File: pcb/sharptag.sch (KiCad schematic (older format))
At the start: 10 parts

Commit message: Layout almost complete. Needs tooling holes.
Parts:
- removed U?: ESP-PSRAM32, Package_SO:SOIC-8_3.9x4.9mm_P1.27mm, symbol Memory_RAM:ESP-PSRAM32
- removed U?: W25Q128JVS, Package_SO:SOIC-8_5.23x5.23mm_P1.27mm, symbol Memory_Flash:W25Q128JVS
- added C1, C14, C15, C18, C20, C3, C6, C7: 100n, Capacitor_SMD:C_0603_1608Metric, symbol Device:C
- added C10, C12, C23, C4: 1u, Capacitor_SMD:C_0603_1608Metric, symbol Device:C
- added C11, C2, C22, C5, C8: 10u, Capacitor_SMD:C_0805_2012Metric, symbol Device:C
- added C13, C19: 2.2u, Capacitor_SMD:C_1206_3216Metric, symbol Device:C
- added C16: 2.2n, Capacitor_SMD:C_0603_1608Metric, symbol Device:C
- added C17: 2.2u, Capacitor_SMD:C_0805_2012Metric, symbol Device:C
- added C21, C9: 22u, Capacitor_SMD:C_0805_2012Metric, symbol Device:C
- added D10, D7, D8, D9: WS2812B, LED_SMD:LED_WS2812B_PLCC4_5.0x5.0mm_P3.2mm, symbol LED:WS2812B
- added D11, D12: ZMM3V3, Diode_SMD:D_MiniMELF, symbol Device:D_Zener
- added D3: B5819W, Diode_SMD:D_SOD-123, symbol Diode:1N5819
- added D4, D5, D6: LED, LED_SMD:LED_0603_1608Metric, symbol Device:LED
- added H1, H2, H3, H4: MountingHole, MountingHole:MountingHole_3.2mm_M3_DIN965, symbol Mechanical:MountingHole
- added J2: Conn_01x10, Connector_FFC-FPC:TE_1-1734839-0_1x10-1MP_P0.5mm_Horizontal, symbol Connector_Generic:Conn_01x10
- added J3: Conn_01x02, Connector_JST:JST_PH_S2B-PH-SM4-TB_1x02-1MP_P2.00mm_Horizontal, symbol Connector_Generic:Conn_01x02
- added J4: Conn_01x04, Connector_JST:JST_SH_SM04B-SRSS-TB_1x04-1MP_P1.00mm_Horizontal, symbol Connector_Generic:Conn_01x04
- added J5, J6: Conn_01x03, Connector_JST:JST_PH_S3B-PH-SM4-TB_1x03-1MP_P2.00mm_Horizontal, symbol Connector_Generic:Conn_01x03
- added JP1: SolderJumper_2_Bridged, Jumper:SolderJumper-2_P1.3mm_Bridged2Bar_RoundedPad1.0x1.5mm, symbol Jumper:SolderJumper_2_Bridged
- added LS1: Speaker, Buzzer_Beeper:MagneticBuzzer_Kobitone_254-EMB84Q-RO, symbol Device:Speaker
- added Q1, Q2, Q3: DMG3415U-7, Package_TO_SOT_SMD:SOT-23, symbol Transistor_FET:DMG2301L
- added Q4: Q_Photo_NPN, Diode_SMD:D_0603_1608Metric, symbol Device:Q_Photo_NPN
- added R1, R10, R16, R22, R23, R26, R3, R5, R8: 10k, Resistor_SMD:R_0603_1608Metric, symbol Device:R
- added R11, R12, R15, R25: 100K, Resistor_SMD:R_0603_1608Metric, symbol Device:R
- added R13, R14, R18: 47k, Resistor_SMD:R_0603_1608Metric, symbol Device:R
- added R17, R20, R21: 1M, Resistor_SMD:R_0603_1608Metric, symbol Device:R
- added R19, R2, R27, R28, R6: 1K, Resistor_SMD:R_0603_1608Metric, symbol Device:R
- added R24: 2.4k, Resistor_SMD:R_0603_1608Metric, symbol Device:R
- added SW1, SW2, SW3, SW4, SW5, SW6: SW_Push, Button_Switch_SMD:SW_SPST_CK_RS282G05A3, symbol Switch:SW_Push
- added SW7: SW_SPDT, Button_Switch_SMD:SW_SPDT_PCM12, symbol Switch:SW_SPDT
- added U2: PAM8302AAS, Package_SO:MSOP-8_3x3mm_P0.65mm, symbol Amplifier_Audio:PAM8302AAS
- added U3: AP2112K-3.3, Package_TO_SOT_SMD:SOT-23-5, symbol Regulator_Linear:AP2112K-3.3
- added U5: MPU-6050, Sensor_Motion:InvenSense_QFN-24_4x4mm_P0.5mm, symbol Sensor_Motion:MPU-6050
- added U6: REG710NA-5, Package_TO_SOT_SMD:SOT-23-6, symbol reg710na:REG710NA-5
- added U7: TPL5110, Package_TO_SOT_SMD:SOT-23-6, symbol Timer:TPL5110
- D1: renamed from D?; LCSC (none) -> C72038
- D2: renamed from D?; LCSC (none) -> C72041
- J1: renamed from J?; footprint (none) -> Connector_USB:USB_C_Receptacle_HRO_TYPE-C-31-M-12; symbol Connector:USB_C_Receptacle_USB2.0 -> sharptag-rescue:USB_C_Receptacle_USB2.0-Connector; LCSC (none) -> C165948
- gave numbers to parts that had none: 5
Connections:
- net BATT_MON: now also U4.18 (IO15), C14.1, R20.1, R21.2; no longer U4.7 (IO04)
- net BOOT0: now also SW2.2
- net D13: now also R16.1
- net GND: now also J1.S1 (SHIELD), C1.2, C10.2, C11.2, C12.2, C13.2, C14.2, C15.2, C16.2, C18.2, C19.2, C2.2, C20.2, C21.2, C22.2, C23.2, C3.2, C4.2, C5.2, C7.2, C8.2, C9.2, D10.3 (VSS), D11.2 (A), D12.2 (A), D4.1 (K), D5.1 (K), D6.1 (K), D7.3 (VSS), D8.3 (VSS), D9.3 (VSS), J2.10 (Pin_10), J2.9 (Pin_9), J3.2 (Pin_2), J4.1 (Pin_1), J5.1 (Pin_1), J6.1 (Pin_1), R11.1, R15.2, R17.1, R21.1, R24.2, R26.2, SW1.1, SW2.1, SW3.1, SW4.1, SW5.1, SW6.1, SW7.2 (B), U2.7 (GND), U3.2 (GND), U5.18 (GND), U6.2 (GND), U7.2 (GND), U7.4 (DONE)
- net IO38_DBLTAP: now also C12.1, R17.2
- net RESET: now also R1.2, SW1.2
- net SCL: now also U4.36 (IO42), J4.4 (Pin_4), R22.2, U5.23 (SCL); no longer U4.28 (IO34)
- net SDA: now also U4.35 (IO41), J4.3 (Pin_3), R23.2, U5.24 (SDA); no longer U4.27 (IO33)
- net SPKR_SD: now reaches U4.19 (IO16)
- net SPKR_SD: now also R15.1, U2.1 (~SD)
- net +3V3: now reaches U4.2 (3V3)
- net +3V3: now also C13.1, C18.1, C20.1, C9.1, J4.2 (Pin_2), J5.2 (Pin_2), J6.2 (Pin_2), JP1.1 (A), Q3.2 (S), R1.1, R10.1, R22.1, R23.1, R25.2, R3.1, R5.1, R8.1, U3.5 (VOUT), U5.13 (VDD), U5.8 (VDDIO), U6.3 (EN), U6.5 (VIN), U7.1 (VDD), U7.6 (EN/ONE_SHOT)
- net AUDIO: now reaches U4.20 (IO17)
- net AUDIO: now also C6.1
- net AD1: now reaches U4.21 (IO18)
- net AD1: now also D12.1 (K), R28.2
- net BUTTON1: now reaches U4.24 (IO21)
- net BUTTON1: now also R5.2, SW4.2
- net BUTTON0: now reaches U4.25 (IO26)
- net BUTTON0: now also R3.2, SW3.2
- net NEOPOWER: now reaches U4.33 (IO39)
- net NEOPOWER: now also Q3.1 (G), R25.1
- net NEOPIXEL: now reaches U4.39 (IO45)
- net NEOPIXEL: now also D7.4 (DIN)
- net BUTTON3: now reaches U4.4 (IO01)
- net BUTTON3: now also R10.2, SW6.2
- net BUTTON2: now reaches U4.5 (IO02)
- net BUTTON2: now also R8.2, SW5.2
- net LIGHT: now reaches U4.6 (IO03)
- net LIGHT: now also Q4.2 (E), R26.1
- net VBUS: now reaches J1.A4 (VBUS), J1.A9 (VBUS), J1.B4 (VBUS), J1.B9 (VBUS)
- net VBUS: now also U1.4 (VCC), C21.1, C5.1, D3.2 (A), Q1.1 (G), R11.2, R19.2, R2.1, R6.2
- net VBAT: now reaches U1.3 (BAT)
- net VBAT: now also C2.1, J3.1 (Pin_1), Q1.3 (D), R20.2
- net at D1.2 (A): now also R2.2; no longer D2.2 (A)
- net MISO renamed CIPO
- net MOSI renamed LCD_DAT
- net LCD_DAT: now also J2.2 (Pin_2)
- net SCK renamed LCD_CS
- net LCD_CS: now also J2.3 (Pin_3)
- new net: D2.2 (A), R6.1
- new net: Q2.1 (G), R12.1, SW7.3 (C)
- new net: D3.1 (K), Q1.2 (S), Q2.2 (S), R12.2
- new net: C17.2, U6.4 (CPUMP-)
- new net: C17.1, U6.6 (CPUMP+)
- new net: C15.1, U5.10 (REGOUT)
- new net: C16.1, U5.20 (CPOUT)
- new net: R13.2, U2.3 (IN+)
- new net: R14.2, U2.4 (IN-)
- new net: LS1.1, U2.5 (OUT+)
- new net: LS1.2, U2.8 (OUT-)
- new net: J5.3 (Pin_3), R27.1
- new net: J6.3 (Pin_3), R28.1
- new net: C7.1, R14.1
- new net: C6.2, R13.1
- new net: D4.2 (A), R16.2
- new net: D5.2 (A), R18.2
- new net: JP1.2 (B), R18.1
- new net: D6.2 (A), R19.1
- new net: D7.2 (DOUT), D8.4 (DIN)
- new net: D8.2 (DOUT), D9.4 (DIN)
- new net: D10.4 (DIN), D9.2 (DOUT)
- new net: R24.1, U7.3 (DELAY/M_DRV)
- new net +5V: C1.1, C19.1, C3.1, C4.1, J2.5 (Pin_5), J2.6 (Pin_6), J2.7 (Pin_7), J2.8 (Pin_8), U6.1 (VOUT)
- new net D1: D11.1 (K), R27.2, U4.27 (IO33)
- new net EXTCOMIN: J2.4 (Pin_4), U7.5 (DRV)
- new net LCD_CLK: J2.1 (Pin_1), U4.28 (IO34)
- new net VDD: C10.1, C11.1, C8.1, Q2.3 (D), U2.6 (VDD), U3.1 (VIN), U3.3 (EN)
- new net VNEO: C22.1, C23.1, D10.1 (VDD), D7.1 (VDD), D8.1 (VDD), D9.1 (VDD), Q3.3 (D), Q4.1 (C)
- no-connect marks 1 -> 8
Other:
- moved on the sheet: D1, D2, J1, R4, R7, R9, U1, U4

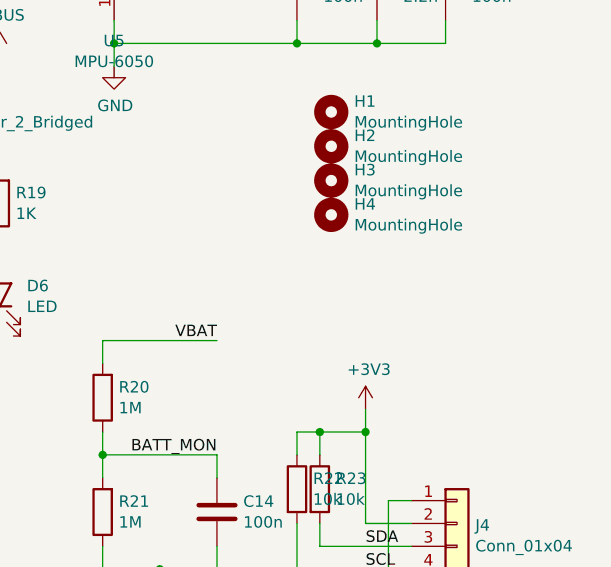
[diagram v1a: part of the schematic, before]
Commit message: Added tooling holes.
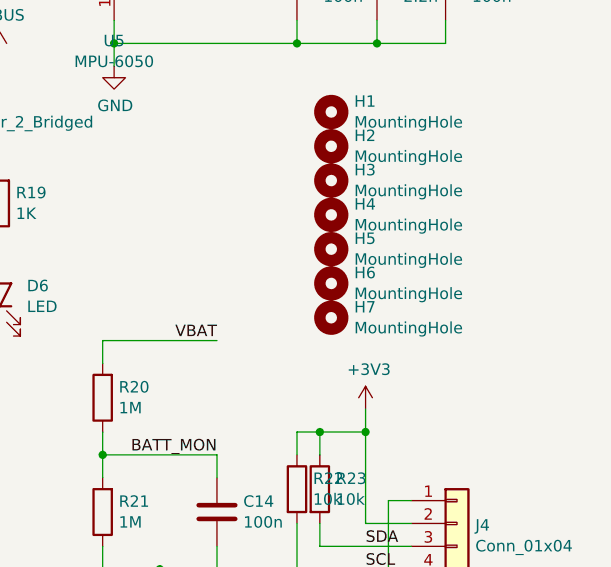
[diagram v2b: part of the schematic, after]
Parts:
- added H5, H6, H7: MountingHole, jlcpcb-tooling:tooling-hole, symbol Mechanical:MountingHole
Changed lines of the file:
@@
 Wire Wire Line
 	5600 2550 4950 2550
+$Comp
+L Mechanical:MountingHole H5
+U 1 1 60612DFD
+P 10500 3600
+F 0 "H5" H 10600 3646 50  0000 L CNN
+F 1 "MountingHole" H 10600 3555 50  0000 L CNN
+F 2 "jlcpcb-tooling:tooling-hole" H 10500 3600 50  0001 C CNN
+F 3 "~" H 10500 3600 50  0001 C CNN
+	1    10500 3600
+	1    0    0    -1
+$EndComp
+$Comp
+L Mechanical:MountingHole H6
+U 1 1 6061317A
+P 10500 3750
+F 0 "H6" H 10600 3796 50  0000 L CNN
+F 1 "MountingHole" H 10600 3705 50  0000 L CNN
+F 2 "jlcpcb-tooling:tooling-hole" H 10500 3750 50  0001 C CNN
+F 3 "~" H 10500 3750 50  0001 C CNN
+	1    10500 3750
+	1    0    0    -1
+$EndComp
+$Comp
+L Mechanical:MountingHole H7
+U 1 1 6061331A
+P 10500 3900
+F 0 "H7" H 10600 3946 50  0000 L CNN
+F 1 "MountingHole" H 10600 3855 50  0000 L CNN
+F 2 "jlcpcb-tooling:tooling-hole" H 10500 3900 50  0001 C CNN
+F 3 "~" H 10500 3900 50  0001 C CNN
+	1    10500 3900
+	1    0    0    -1
+$EndComp
 $EndSCHEMATC

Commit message: Adding manufacturing data
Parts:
- D1: value LED -> LED_YELLOW
- D2, D6: value LED -> LED_BLUE
- D4: value LED -> LED_RED
- D5: value LED -> LED_GREEN
- LS1: LCSC (none) -> C94599
- U3: LCSC (none) -> C51118
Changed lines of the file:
@@
 P 1000 6600
 F 0 "D1" V 1039 6482 50  0000 R CNN
-F 1 "LED" V 948 6482 50  0000 R CNN
+F 1 "LED_YELLOW" V 948 6482 50  0000 R CNN
 F 2 "LED_SMD:LED_0603_1608Metric" H 1000 6600 50  0001 C CNN
 F 3 "~" H 1000 6600 50  0001 C CNN
@@
 P 2700 6600
 F 0 "D2" V 2739 6482 50  0000 R CNN
-F 1 "LED" V 2648 6482 50  0000 R CNN
+F 1 "LED_BLUE" V 2648 6482 50  0000 R CNN
 F 2 "LED_SMD:LED_0603_1608Metric" H 2700 6600 50  0001 C CNN
 F 3 "~" H 2700 6600 50  0001 C CNN
@@
 F 2 "Package_TO_SOT_SMD:SOT-23-5" H 5450 7175 50  0001 C CNN
 F 3 "https://www.diodes.com/assets/Datasheets/AP2112.pdf" H 5450 6950 50  0001 C CNN
+F 4 "C51118" H 5450 6850 50  0001 C CNN "LCSC"
 	1    5450 6850
 	1    0    0    -1
@@
 P 8050 3800
 F 0 "D4" V 8089 3682 50  0000 R CNN
-F 1 "LED" V 7998 3682 50  0000 R CNN
+F 1 "LED_RED" V 7998 3682 50  0000 R CNN
 F 2 "LED_SMD:LED_0603_1608Metric" H 8050 3800 50  0001 C CNN
 F 3 "~" H 8050 3800 50  0001 C CNN
@@
 P 8550 3800
 F 0 "D5" V 8589 3682 50  0000 R CNN
-F 1 "LED" V 8498 3682 50  0000 R CNN
+F 1 "LED_GREEN" V 8498 3682 50  0000 R CNN
 F 2 "LED_SMD:LED_0603_1608Metric" H 8550 3800 50  0001 C CNN
 F 3 "~" H 8550 3800 50  0001 C CNN
@@
 P 9050 3800
 F 0 "D6" V 9089 3682 50  0000 R CNN
-F 1 "LED" V 8998 3682 50  0000 R CNN
+F 1 "LED_BLUE" V 8998 3682 50  0000 R CNN
 F 2 "LED_SMD:LED_0603_1608Metric" H 9050 3800 50  0001 C CNN
 F 3 "~" H 9050 3800 50  0001 C CNN
@@
 F 2 "Buzzer_Beeper:MagneticBuzzer_Kobitone_254-EMB84Q-RO" H 6250 4850 50  0001 C CNN
 F 3 "~" H 6240 5000 50  0001 C CNN
+F 4 " C94599" H 6250 5050 50  0001 C CNN "LCSC"
 	1    6250 5050
 	1    0    0    -1
